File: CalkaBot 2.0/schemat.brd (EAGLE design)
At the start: 94.4 x 101.8 mm, 48 parts, among them IC1 TB6612FNG, IC2 LM339D, IC3 7806DT, Q1 16MHz, X1 MINI-USB-32005-301

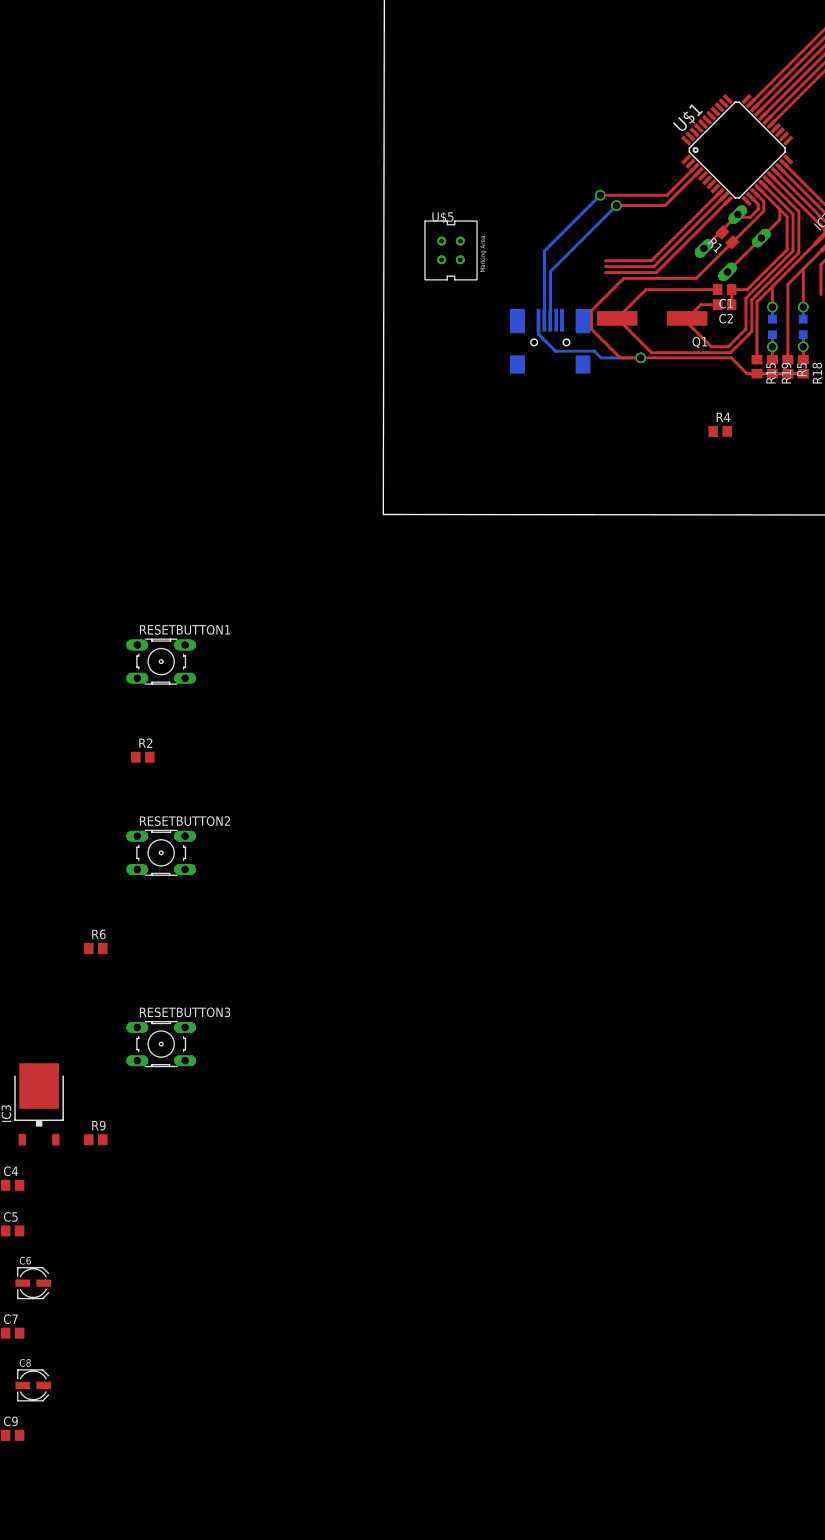
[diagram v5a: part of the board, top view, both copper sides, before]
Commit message: podłączenie przycisków teraz
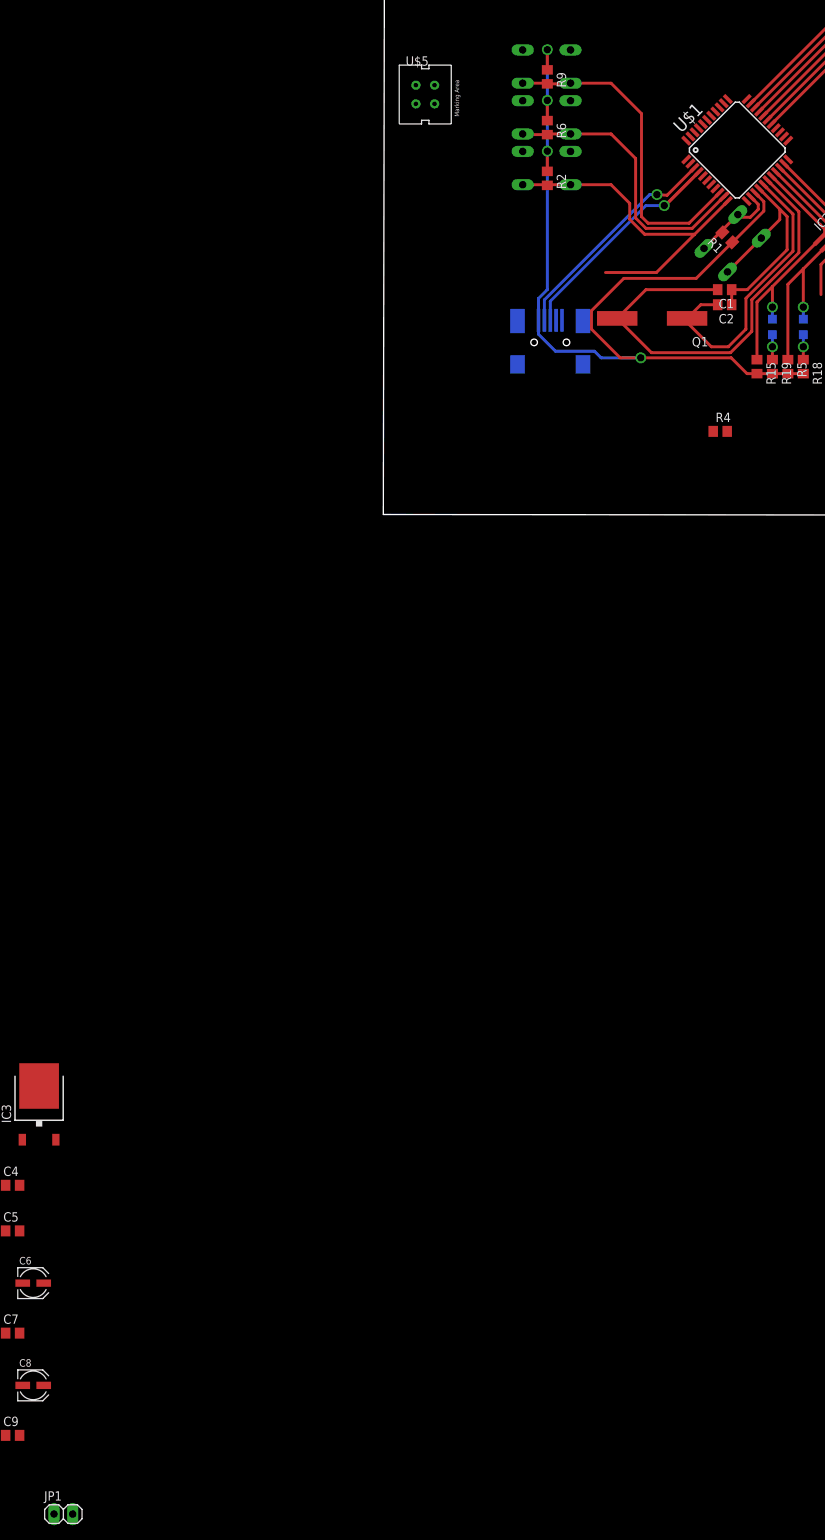
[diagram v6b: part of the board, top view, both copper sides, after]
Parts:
- removed RESETBUTTON1, RESETBUTTON2, RESETBUTTON3: (no value), switch-omron:B3F-10XX
- added BUT1, BUT2, BUT3: (no value), switch-omron:B3F-10XX
- added JP1: (no value), pinhead:1X02
- moved R9 157.0 mm to (24.4, 48.4), turned to 270 degrees
- moved R6 127.4 mm to (24.4, 41.5), turned to 270 degrees
- moved R2 96.0 mm to (24.4, 34.6), turned to 270 degrees
- moved U$5 21.5 mm to (7.80, 46.0)
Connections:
- removed net GND2: RESETBUTTON2.1, RESETBUTTON2.2
- removed net GND3: RESETBUTTON3.1, RESETBUTTON3.2
- removed net VCC2: R6.1
- removed net VCC3: R9.1
- net GND: now also BUT1.1, BUT1.2, BUT2.1, BUT2.2, BUT3.1, BUT3.2, JP1.1; no longer RESETBUTTON1.1, RESETBUTTON1.2
- net MISO: now also BUT1.3, BUT1.4, R2.2; no longer R6.2, RESETBUTTON2.3, RESETBUTTON2.4
- net MOSI: now also BUT2.3, BUT2.4, R6.2; no longer R2.2, RESETBUTTON1.3, RESETBUTTON1.4
- net SCK: now also BUT3.3, BUT3.4; no longer RESETBUTTON3.3, RESETBUTTON3.4
- net VCC: now also R6.1, R9.1
- net VM: now also JP1.2
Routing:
- net VCC: track 99.4 -> 144.9 mm, vias 1 -> 4
- net MISO: track 20.7 -> 48.2 mm
- net SCK: track 19.3 -> 44.8 mm
- net MOSI: track 21.0 -> 40.2 mm
- net D+: track 31.6 -> 36.5 mm
- net D-: track 34.5 -> 30.7 mm

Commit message: nie ma miejsca na usb, pcb prawie skończone
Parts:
- removed U$3, U$4, U$5, U$6: CNY70, cny70:4
- added C10: 1uF, rcl:UD-4X5,8_NICHICON
- added JP2, JP3: (no value), pinhead:1X05
- added LED5, LED6: (no value), led:CHIP-LED0805
- added R12, R22: 220R, rcl:R0805
- added R25, R26: 22R, rcl:R0805
- added SW1: (no value), special:EDG-01
- RESETBUTTON: value (none) -> DTS-3; device switch-omron:B3F-10XX -> switch-tact (1):DTS-3
- moved C9 233.4 mm to (75.0, 61.9), turned to 180 degrees
- moved JP1 223.2 mm to (28.6, 64.9), flipped to the bottom, turned to 180 degrees
- moved C7 213.5 mm to (62.8, 59.9), turned to 270 degrees
- moved C8 206.6 mm to (39.4, 58.8), turned to 135 degrees
- moved C6 188.1 mm to (34.9, 54.4), turned to 135 degrees
- moved C4 186.7 mm to (41.9, 61.2), turned to 135 degrees
- moved C5 179.6 mm to (32.5, 51.9), turned to 135 degrees
- moved IC3 166.8 mm to (26.1, 59.7), turned to 90 degrees
- moved X1 82.0 mm to (88.5, 63.9), turned to 270 degrees
- moved R4 63.8 mm to (90.6, 47.6), turned to 270 degrees
- moved C3 51.4 mm to (21.6, 50.8)
- moved R8 44.7 mm to (88.2, 47.7), turned to 270 degrees
- moved R14 37.3 mm to (67.8, 9.50), turned to 270 degrees
- moved RESETBUTTON 37.1 mm to (24.8, 53.4), turned to 180 degrees
- moved R11 36.0 mm to (92.8, 47.6), turned to 270 degrees
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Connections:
- net N$8 renamed I/O11
- net X renamed I/O12
- net XX renamed I/O9
- net XXX renamed I/O8
- net XXXX renamed I/O7
- removed net ID: X1.2
- removed net N$10: U$1.6
- removed net N$11: U$1.42
- removed net N$14: U$1.5
- removed net N$2: U$1.7
- removed net N$3: C4.2, IC3.2
- removed net PGND1: IC1.3
- removed net PGND1': IC1.4
- removed net PGND2: IC1.9
- removed net PGND2': IC1.10
- new net AO1: IC1.1, IC1.2
- new net AO2: IC1.5, IC1.6
- new net BO1: IC1.11, IC1.12
- new net BO2: IC1.7, IC1.8
- new net I/O1: U$1.41
- new net I/O10: U$1.33
- new net I/O2: U$1.40
- new net I/O3: U$1.39
- new net I/O4: U$1.38
- new net I/O5: U$1.37
- new net I/O6: U$1.36
- new net N$12: JP2.3, JP3.3, R25.1, X1.3
- new net N$20: JP2.4, JP3.4, R26.1, X1.4
- new net N$7: LED5.A, R12.1
- new net N$9: LED6.A, R22.1
- new net PIN: JP1.2, SW1.1
- new net UCAP: C10.+, U$1.6
- new net VBUS: JP2.5, JP3.5, U$1.7, X1.5
- net D+: now also R25.2; no longer X1.3
- net D-: now also R26.2; no longer X1.4
- net GND: now also C10.-, IC1.10, IC1.3, IC1.4, IC1.9, JP2.1, JP2.2, JP3.1, JP3.2, LED5.C, LED6.C, U$1.5, X1.2; no longer RESETBUTTON.1, U$3.E, U$3.K, U$4.E, U$4.K, U$5.E, U$5.K, U$6.E, U$6.K
- net N$1: no longer U$3.A
- net N$19: no longer U$4.A
- net N$23: no longer U$5.A
- net N$27: no longer U$6.A
- net RST: now also RESETBUTTON.1; no longer RESETBUTTON.3, RESETBUTTON.4
- net S1: no longer U$3.C
- net S2: no longer U$4.C
- net S3: no longer U$5.C
- net S4: no longer U$6.C
- net VCC: now also C4.2, IC3.2, R12.2, U$1.42; no longer X1.5
- net VM: now also R22.2, SW1.2; no longer JP1.2
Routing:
- net GND: track 54.2 -> 387.5 mm, vias 0 -> 1
- net VCC: track 144.9 -> 252.1 mm
- net VM: track 0.00 -> 80.7 mm, vias 0 -> 3
- net RST: track 12.0 -> 68.5 mm, vias 0 -> 1
- net VBUS: track 0.00 -> 36.9 mm, vias 0 -> 1
- net PIN: track 0.00 -> 26.4 mm
- net S4: track 2.63 -> 26.1 mm
- net D+: track 36.5 -> 15.7 mm, vias 1 -> 0
- net N$7: track 0.00 -> 20.7 mm, vias 0 -> 1
- net S3: track 2.90 -> 22.4 mm
- net D-: track 30.7 -> 12.2 mm, vias 1 -> 0
- net N$20: track 0.00 -> 18.0 mm, vias 0 -> 1
- net SCK: track 44.8 -> 29.0 mm
- net N$12: track 0.00 -> 15.0 mm, vias 0 -> 1
- net I/O1: track 0.00 -> 15.0 mm, vias 0 -> 1
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
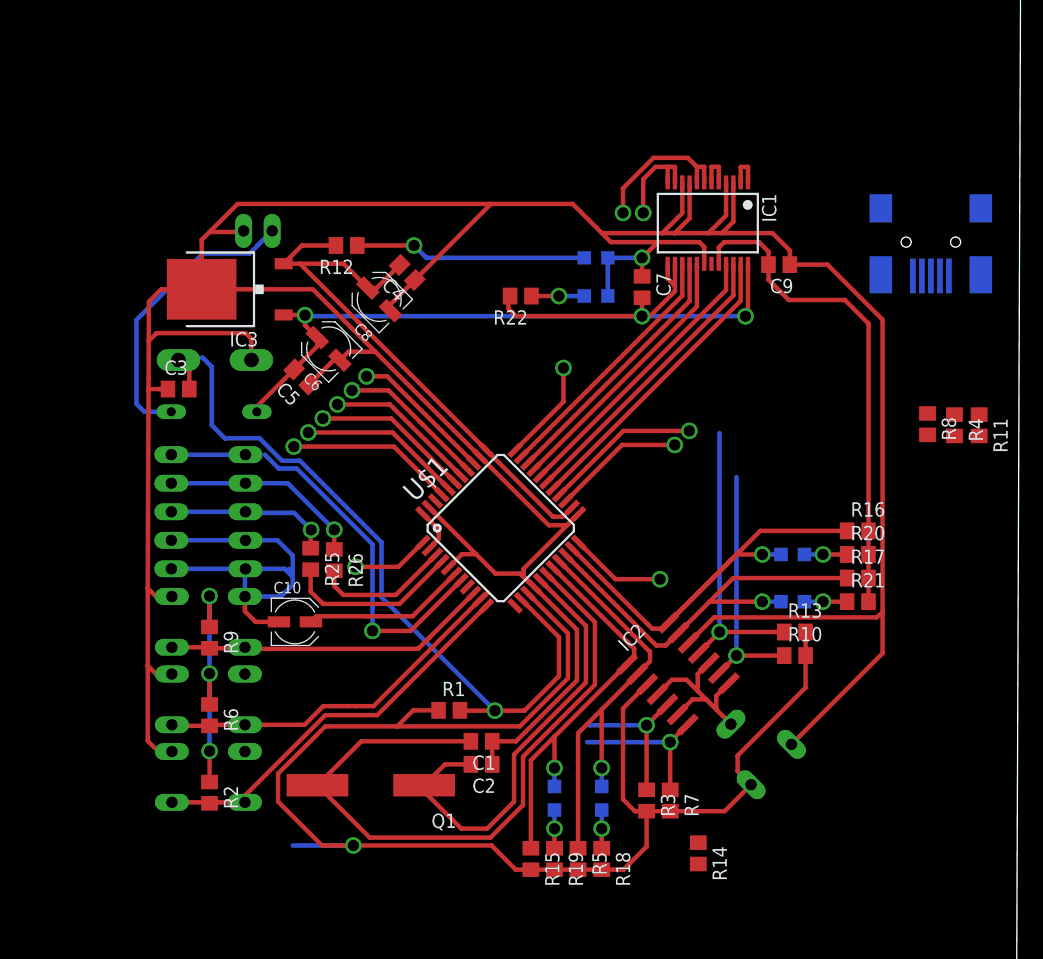
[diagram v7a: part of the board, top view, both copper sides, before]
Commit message: potrzebne wyjscia do czujnikow odleglosci i płytka z gniazdem usb
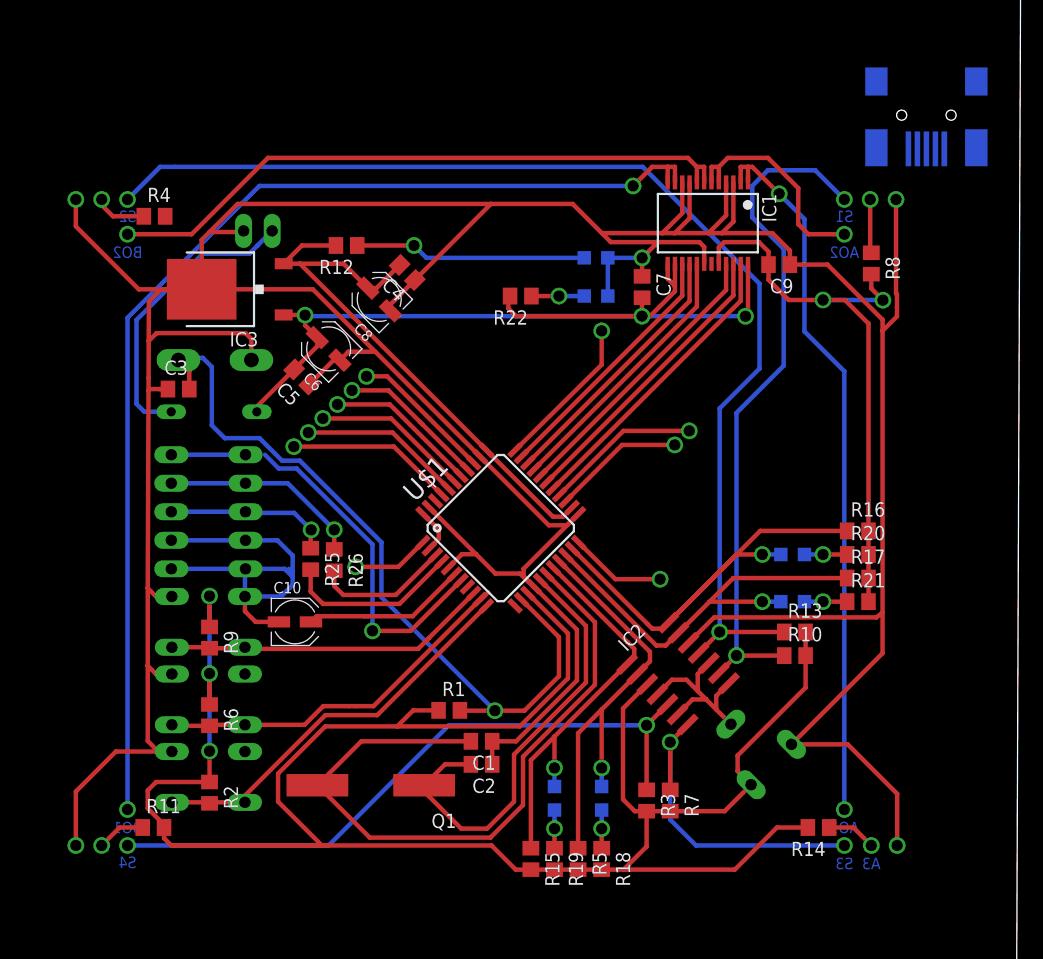
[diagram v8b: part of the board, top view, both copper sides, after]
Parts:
- moved R11 81.8 mm to (19.3, 11.8), turned to 0 degrees
- moved R4 73.6 mm to (19.4, 66.2), turned to 0 degrees
- moved R8 15.1 mm to (83.2, 62.0)
- moved X1 11.3 mm to (88.1, 75.2)
- moved R14 10.9 mm to (78.5, 11.8), turned to 180 degrees
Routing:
- net BO1: track 9.05 -> 100.8 mm, vias 1 -> 2
- net S4: track 26.1 -> 102.7 mm, vias 1 -> 2
- net AO1: track 3.42 -> 64.4 mm, vias 0 -> 2
- net GND: track 387.5 -> 446.3 mm, vias 1 -> 5
- net VCC: track 252.1 -> 297.7 mm, vias 4 -> 5
- net S1: track 13.8 -> 59.2 mm, vias 1 -> 2
- net BO2: track 13.6 -> 57.2 mm
- net S3: track 22.4 -> 61.0 mm, vias 1 -> 2
- net AO2: track 3.42 -> 19.6 mm, vias 0 -> 1
- net S2: track 13.9 -> 29.8 mm, vias 1 -> 2
- net N$19: track 0.00 -> 4.85 mm, vias 0 -> 1
- net I/O10: track 9.10 -> 13.8 mm
- net N$1: track 0.00 -> 4.66 mm, vias 0 -> 1
- net N$27: track 0.00 -> 4.41 mm, vias 0 -> 1
- net N$23: track 0.00 -> 4.31 mm, vias 0 -> 1
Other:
- board text added: "A3"
- board text added: "AO1"
- board text added: "AO2"
- board text added: "BO1"
- board text added: "BO2"
- board text added: "S1"
- board text added: "S2"
- board text added: "S3"
- board text added: "S4"
